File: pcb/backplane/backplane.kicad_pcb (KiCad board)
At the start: 2 copper layers, 101.6 x 101.6 mm, 85 parts, among them U2 IFX9201SGAUMA1, U3 IFX9201SGAUMA1, U4 IFX9201SGAUMA1, U5 PREC004SAAN-RC, U6 IFX9201SGAUMA1

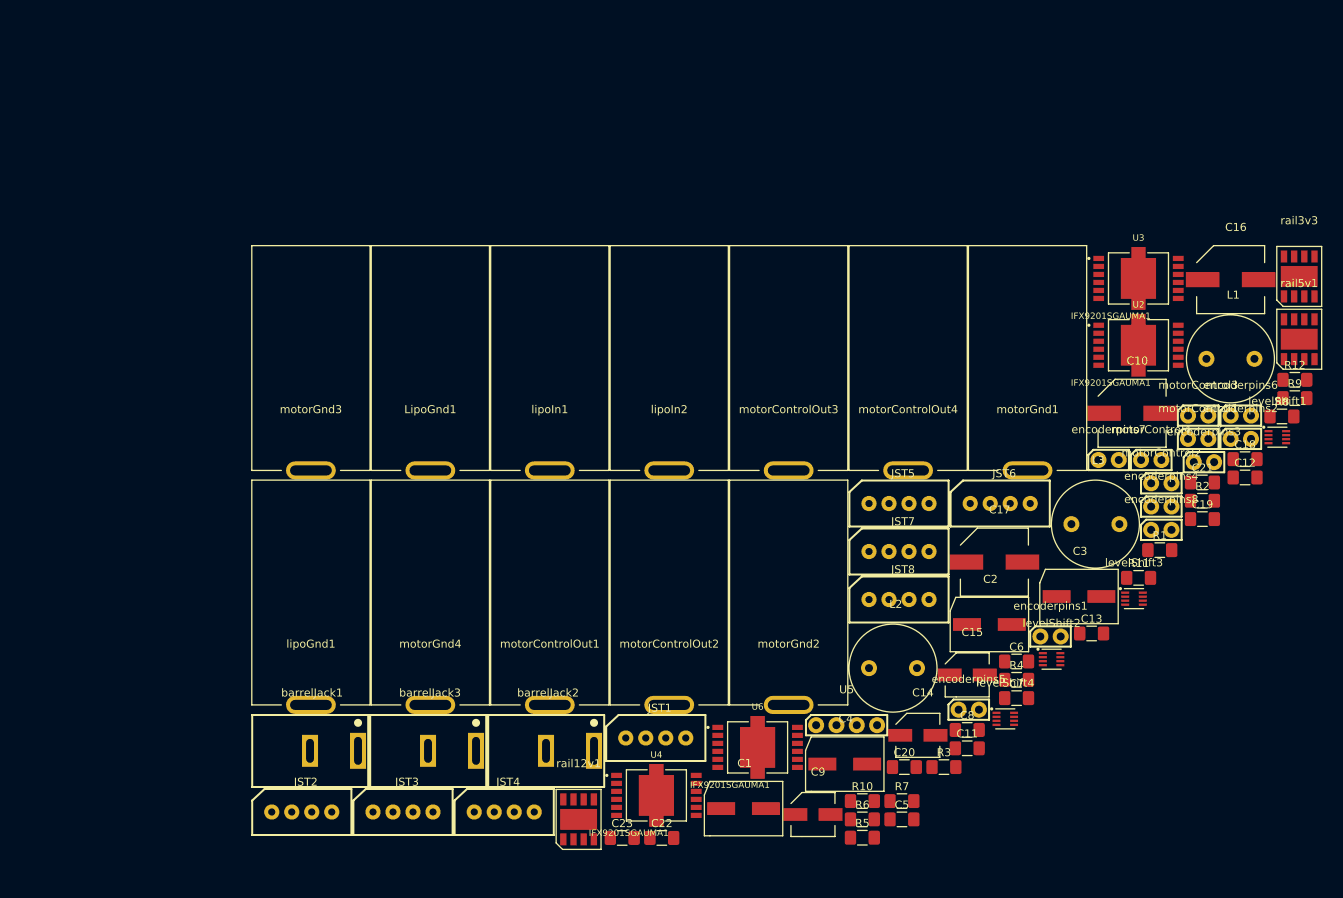
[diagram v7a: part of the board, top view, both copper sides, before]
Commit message: updates
finished choosing parts and completed the schematic
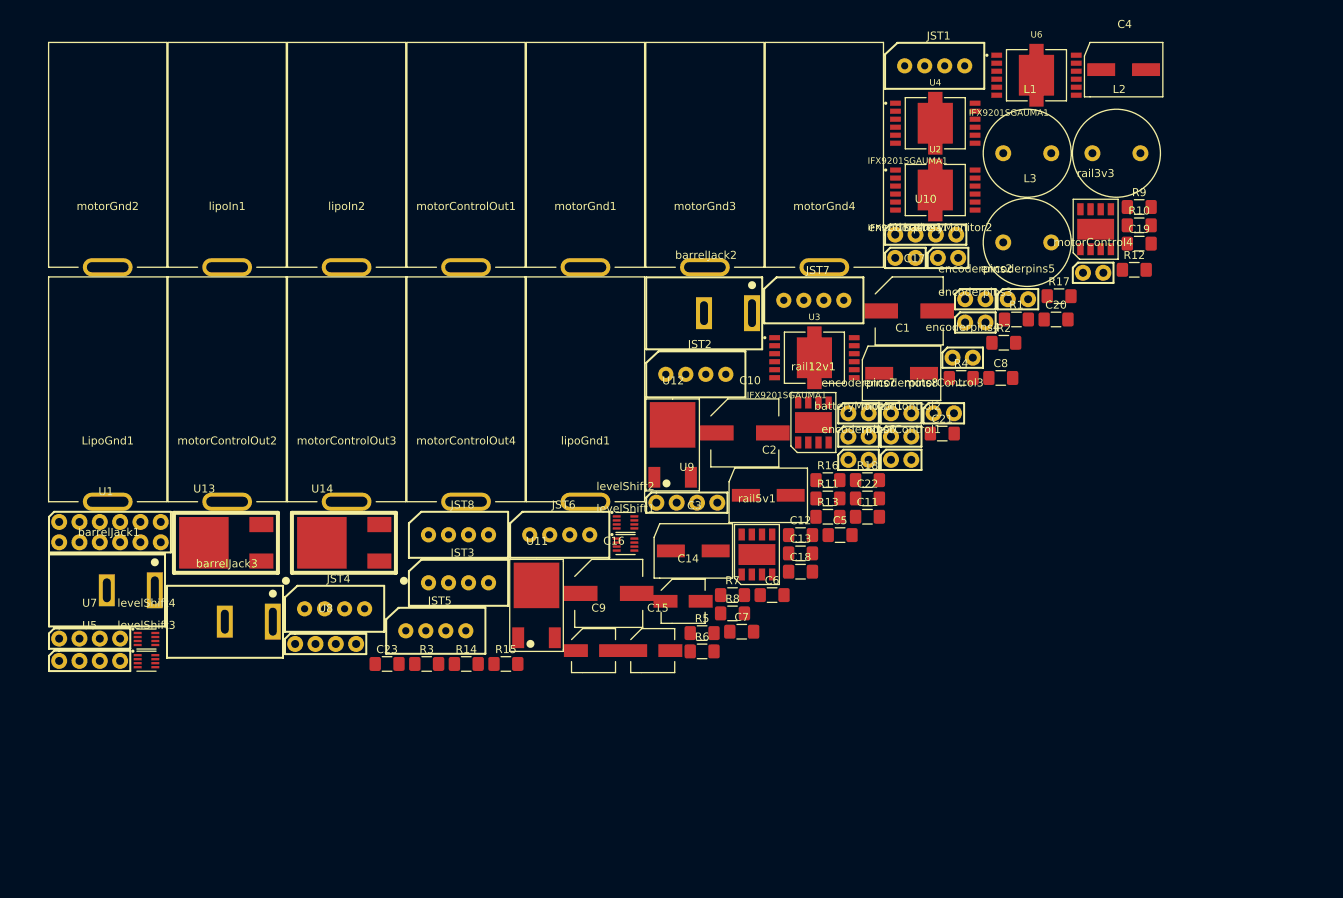
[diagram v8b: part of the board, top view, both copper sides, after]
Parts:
- added R13: 10K, Resistor_SMD:R_1206_3216Metric_Pad1.42x1.75mm_HandSolder, F.Cu at (224.5, 34.0)
- added R14: 42K, Resistor_SMD:R_1206_3216Metric_Pad1.42x1.75mm_HandSolder, F.Cu at (179.3, 52.4)
- added R15: 10K, Resistor_SMD:R_1206_3216Metric_Pad1.42x1.75mm_HandSolder, F.Cu at (184.2, 52.4)
- added R16: 10K, Resistor_SMD:R_1206_3216Metric_Pad1.42x1.75mm_HandSolder, F.Cu at (224.5, 29.4)
- added R17: 42K, Resistor_SMD:R_1206_3216Metric_Pad1.42x1.75mm_HandSolder, F.Cu at (253.4, 6.40)
- added R18: 10K, Resistor_SMD:R_1206_3216Metric_Pad1.42x1.75mm_HandSolder, F.Cu at (229.4, 29.4)
- added U1: PRPC006DAAN-RC, backplane:PRPC006DAAN-RC, F.Cu at (132.2, 35.9)
- added U10: PREC004SAAN-RC, backplane:PREC004SAAN-RC, F.Cu at (236.7, -1.30)
- added U11: DMP3028LK3-13, backplane:DMP3028LK3-13, F.Cu at (188.1, 42.5)
- added U12: DMP3028LK3-13, backplane:DMP3028LK3-13, F.Cu at (205.1, 22.5)
- added U13: NTD4969NT4G, backplane:NTD4969NT4G, F.Cu at (146.5, 37.2)
- added U14: NTD4969NT4G, backplane:NTD4969NT4G, F.Cu at (161.2, 37.2)
- added U7: PREC004SAAN-RC, backplane:PREC004SAAN-RC, F.Cu at (132.2, 49.2)
- added U8: PREC004SAAN-RC, backplane:PREC004SAAN-RC, F.Cu at (161.7, 49.9)
- added U9: PREC004SAAN-RC, backplane:PREC004SAAN-RC, F.Cu at (206.9, 32.2)
- added batteryMonitor1: PREC002SAAN-RC, backplane:PREC002SAAN-RC, F.Cu at (228.3, 22.7)
- added batteryMonitor2: PREC002SAAN-RC, backplane:PREC002SAAN-RC, F.Cu at (239.5, 0.34)
- moved levelShift3 123.7 mm to (139.3, 52.0)
- moved levelShift4 107.8 mm to (139.3, 49.3)
- moved motorGnd2 101.2 mm to (134.5, 2.78)
- moved U5 95.0 mm to (132.2, 52.0)
- moved C4 93.5 mm to (261.5, -21.9)
- moved JST1 91.0 mm to (237.8, -22.4)
- moved U4 91.0 mm to (237.9, -15.2)
- moved U6 91.0 mm to (250.6, -21.2)
- moved C16 87.1 mm to (197.1, 43.5)
- moved levelShift1 82.6 mm to (199.2, 37.4)
- moved R10 79.9 mm to (263.4, -2.46)
- moved JST2 73.6 mm to (208.0, 16.2)
- moved motorGnd4 73.6 mm to (224.0, 2.78)
- moved R8 73.0 mm to (212.6, 46.0)
- moved rail5v1 72.9 mm to (215.6, 38.7)
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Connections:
- lipoIn1 pad 1: +14v8 -> liPo1
- lipoIn2 pad 1: +14v8 -> lipo2
